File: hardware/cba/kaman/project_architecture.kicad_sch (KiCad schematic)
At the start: 0 parts

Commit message: hw(schematic): Draw the schematic part of ESP32 C6
Add the ESP32 C6 and it's necessary part's needed for it to function such as the decoupling caps, the auto program circuit and buttons needed
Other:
- added sheet IO Port (io_port.kicad_sch)
- added sheet Interface (interface.kicad_sch)
- added sheet MCU & GPS (mcu_gps.kicad_sch)
- added sheet Power (power.kicad_sch)
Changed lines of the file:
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@@
 (kicad_sch
-	(version 20250114)
+	(version 20260306)
 	(generator "eeschema")
-	(generator_version "9.0")
+	(generator_version "10.0")
 	(paper "A4")
+	(sheet
+		(at 115.57 123.19)
+		(size 27.94 17.78)
+		(exclude_from_sim no)
+		(in_bom yes)
+		(on_board yes)
+		(dnp no)
+		(fields_autoplaced yes)
+		(stroke
+			(width 0.1524)
+			(type solid)
+		)
+		(fill
+			(color 0 0 0 0)
+		)
+		(property "Sheetname" "Power"
+			(at 115.57 122.4784 0)
+			(show_name no)
+			(do_not_autoplace no)
+			(effects
+				(font
+					(size 1.27 1.27)
+				)
+				(justify left bottom)
+			)
+		)
+		(property "Sheetfile" "power.kicad_sch"
+			(at 115.57 141.5546 0)
+			(show_name no)
+			(do_not_autoplace no)
+			(effects
+				(font
+					(size 1.27 1.27)
+				)
+				(justify left top)
+			)
+		)
+		(instances
+			(project "Template"
+				(path "/b7abe575-2b7a-4e47-9046-9769d7102f9d/c3e404eb-2e1f-4ab9-8da3-bc1a9ff0af28"
+					(page "7")
+				)
+			)
+		)
+	)
+	(sheet
+		(at 115.57 101.6)
+		(size 27.94 16.51)
+		(exclude_from_sim no)
+		(in_bom yes)
+		(on_board yes)
+		(dnp no)
+		(fields_autoplaced yes)
+		(stroke
+			(width 0.1524)
+			(type solid)
+		)
+		(fill
+			(color 0 0 0 0)
+		)
+		(property "Sheetname" "Interface"
+			(at 115.57 100.8884 0)
+			(show_name no)
+			(do_not_autoplace no)
+			(effects
+				(font
+					(size 1.27 1.27)
+				)
+				(justify left bottom)
+			)
+		)
+		(property "Sheetfile" "interface.kicad_sch"
+			(at 115.57 118.6946 0)
+			(show_name no)
+			(do_not_autoplace no)
+			(effects
+				(font
+					(size 1.27 1.27)
+				)
+				(justify left top)
+			)
+		)
+		(instances
+			(project "Template"
+				(path "/b7abe575-2b7a-4e47-9046-9769d7102f9d/c3e404eb-2e1f-4ab9-8da3-bc1a9ff0af28"
+					(page "6")
+				)
+			)
+		)
+	)
+	(sheet
+		(at 115.57 78.74)
+		(size 27.94 17.78)
+		(exclude_from_sim no)
+		(in_bom yes)
+		(on_board yes)
+		(dnp no)
+		(fields_autoplaced yes)
+		(stroke
+			(width 0.1524)
+			(type solid)
+		)
+		(fill
+			(color 0 0 0 0)
+		)
+		(property "Sheetname" "IO Port"
+			(at 115.57 78.0284 0)
+			(show_name no)
+			(do_not_autoplace no)
+			(effects
+				(font
+					(size 1.27 1.27)
+				)
+				(justify left bottom)
+			)
+		)
+		(property "Sheetfile" "io_port.kicad_sch"
+			(at 115.57 97.1046 0)
+			(show_name no)
+			(do_not_autoplace no)
+			(effects
+				(font
+					(size 1.27 1.27)
+				)
+				(justify left top)
+			)
+		)
+		(instances
+			(project "Template"
+				(path "/b7abe575-2b7a-4e47-9046-9769d7102f9d/c3e404eb-2e1f-4ab9-8da3-bc1a9ff0af28"
+					(page "5")
+				)
+			)
+		)
+	)
+	(sheet
+		(at 115.57 57.15)
+		(size 27.94 16.51)
+		(exclude_from_sim no)
+		(in_bom yes)
+		(on_board yes)
+		(dnp no)
+		(fields_autoplaced yes)
+		(stroke
+			(width 0.1524)
+			(type solid)
+		)
+		(fill
+			(color 0 0 0 0)
+		)
+		(property "Sheetname" "MCU & GPS"
+			(at 115.57 56.4384 0)
+			(show_name no)
+			(do_not_autoplace no)
+			(effects
+				(font
+					(size 1.27 1.27)
+				)
+				(justify left bottom)
+			)
+		)
+		(property "Sheetfile" "mcu_gps.kicad_sch"
+			(at 115.57 74.2446 0)
+			(show_name no)
+			(do_not_autoplace no)
+			(effects
+				(font
+					(size 1.27 1.27)
+				)
+				(justify left top)
+			)
+		)
+		(instances
+			(project "Template"
+				(path "/b7abe575-2b7a-4e47-9046-9769d7102f9d/c3e404eb-2e1f-4ab9-8da3-bc1a9ff0af28"
+					(page "4")
+				)
+			)
+		)
+	)
 )

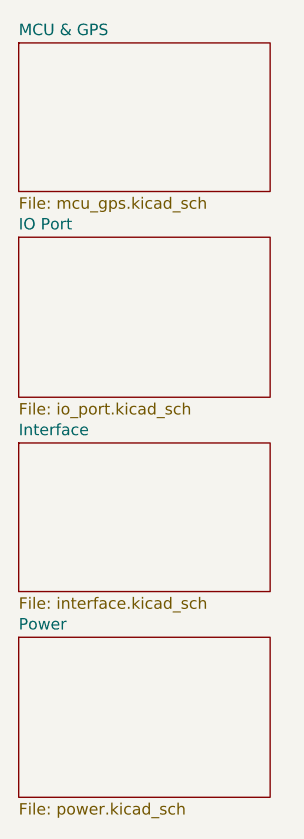
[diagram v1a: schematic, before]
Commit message: hw(schematic): add the power section
Three power sources USB, DC Jack and simple 2.54mm connector with a
schottkey diode on USB and simple ones to block reverse current into a
AZ1117 and outputs 3.3v
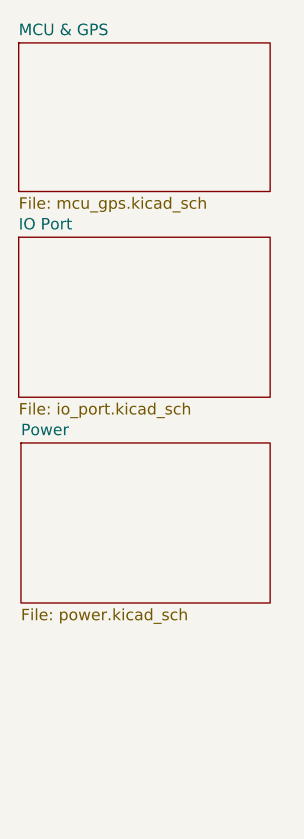
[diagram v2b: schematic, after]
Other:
- removed sheet Interface
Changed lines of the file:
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@@
 	(paper "A4")
 	(sheet
-		(at 115.57 123.19)
-		(size 27.94 17.78)
+		(at 115.824 101.6)
+		(size 27.686 17.78)
 		(exclude_from_sim no)
 		(in_bom yes)
@@
 		)
 		(property "Sheetname" "Power"
-			(at 115.57 122.4784 0)
+			(at 115.824 100.8884 0)
 			(show_name no)
 			(do_not_autoplace no)
@@
 		)
 		(property "Sheetfile" "power.kicad_sch"
-			(at 115.57 141.5546 0)
+			(at 115.824 119.9646 0)
 			(show_name no)
 			(do_not_autoplace no)
@@
 				)
 			)
-		)
-	)
-	(sheet
-		(at 115.57 101.6)
-		(size 27.94 16.51)
-		(exclude_from_sim no)
-		(in_bom yes)
-		(on_board yes)
-		(dnp no)
-		(fields_autoplaced yes)
-		(stroke
-			(width 0.1524)
-			(type solid)
-		)
-		(fill
-			(color 0 0 0 0)
-		)
-		(property "Sheetname" "Interface"
-			(at 115.57 100.8884 0)
-			(show_name no)
-			(do_not_autoplace no)
-			(effects
-				(font
-					(size 1.27 1.27)
-				)
-				(justify left bottom)
-			)
-		)
-		(property "Sheetfile" "interface.kicad_sch"
-			(at 115.57 118.6946 0)
-			(show_name no)
-			(do_not_autoplace no)
-			(effects
-				(font
-					(size 1.27 1.27)
-				)
-				(justify left top)
-			)
-		)
-		(instances
-			(project "Template"
-				(path "/b7abe575-2b7a-4e47-9046-9769d7102f9d/c3e404eb-2e1f-4ab9-8da3-bc1a9ff0af28"
-					(page "6")
-				)
-			)
